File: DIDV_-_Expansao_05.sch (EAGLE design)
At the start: 83 parts, among them U101 TLC5940QPWPREP, U201 TLC5940QPWPREP

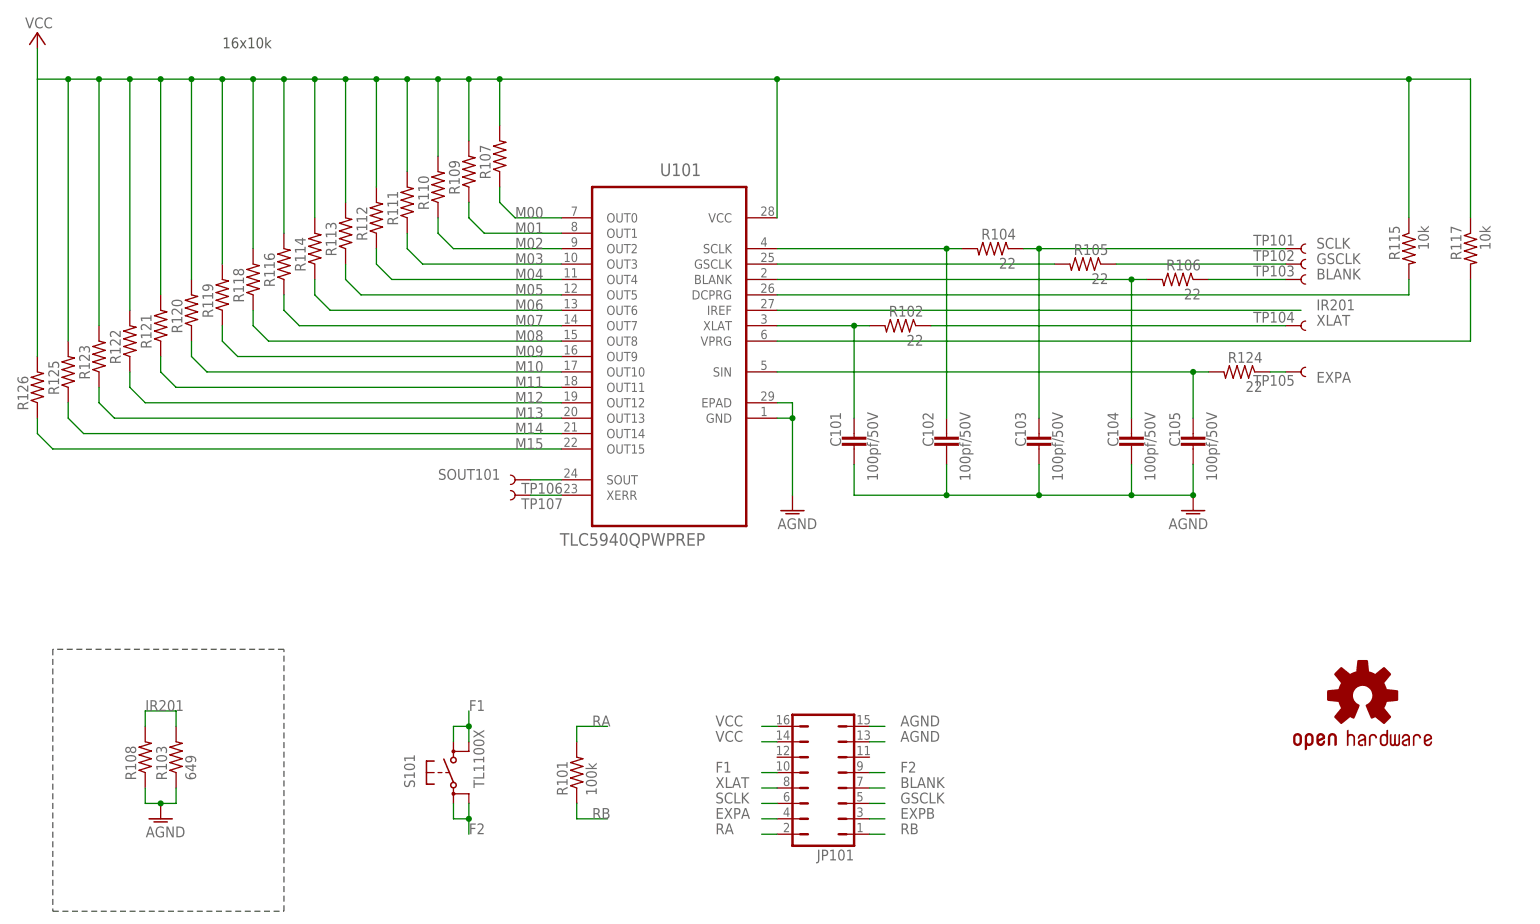
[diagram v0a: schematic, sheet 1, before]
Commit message: Revisão 7:
-  Alterações necessárias para adequação às necessidades dos exemplos de controle que temos.
-  Revisão da forma de filtragem de sinais digitais
-  Algumas nomenclaturas ainda estão erradas, deverão ser corrigidas com o andamento da implementação.
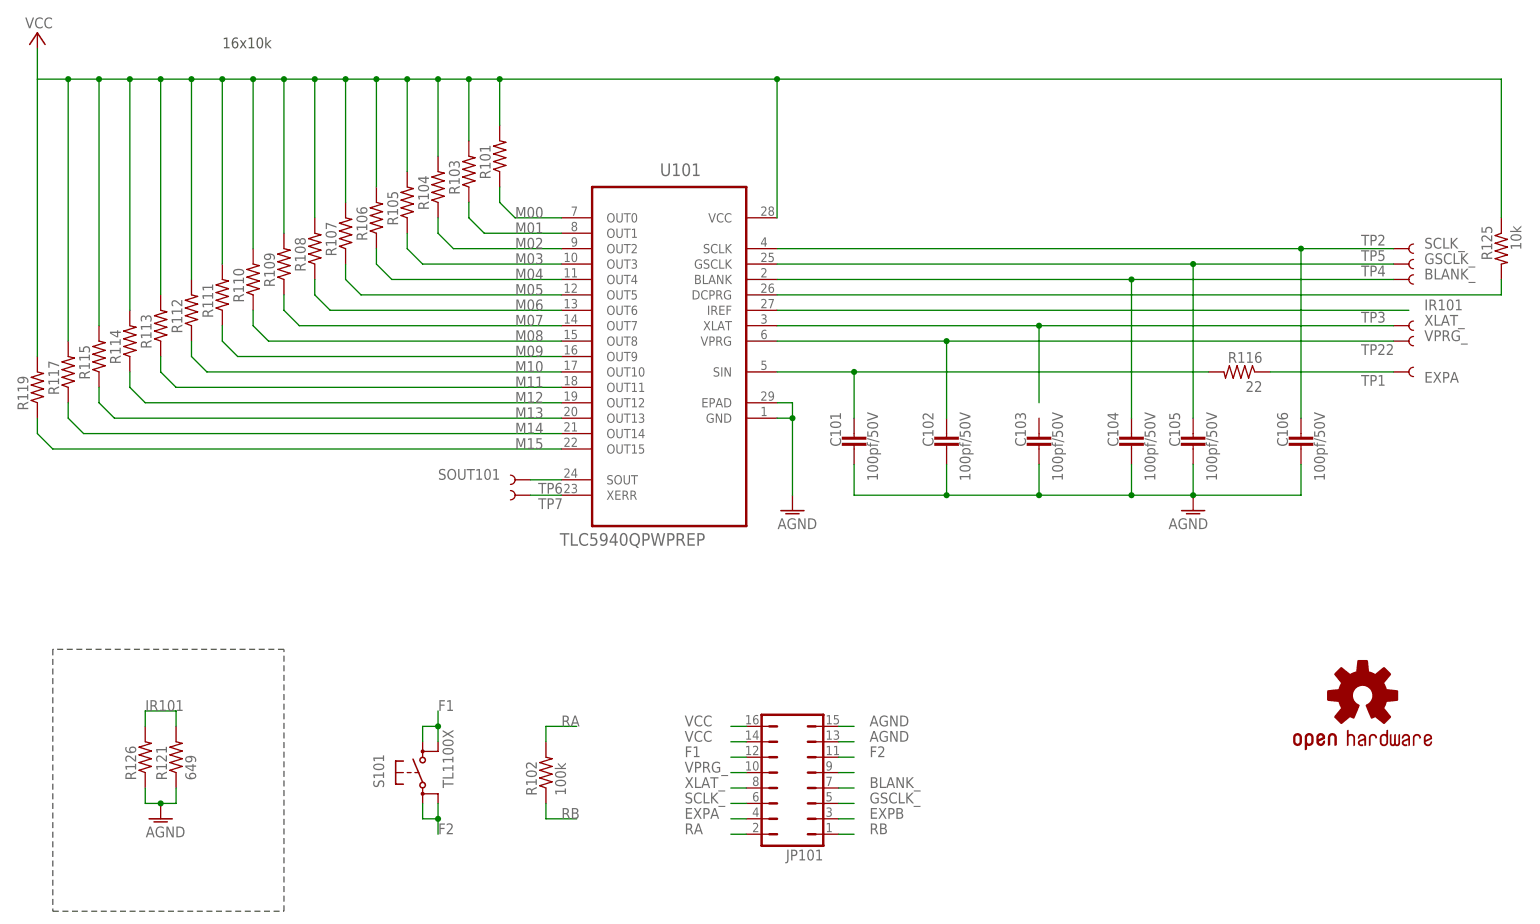
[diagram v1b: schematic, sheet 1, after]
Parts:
- removed R118, R120, R122, R123, R217: (no value), rcl:R-US_R0805
- removed R124, R222, R223: 22, rcl:R-US_R0603
- removed R219: 10k, rcl:R-US_R0603
- removed R221: 649, rcl:R-US_R0805
- removed TP101, TP102, TP103, TP104, TP105, TP15, TP16, TP17, TP18, TP19, TP20: TEST-POINT3X4, SparkFun-Passives:TEST-POINT3X4
- added C106, C207: 100pf/50V, rcl:C-EUC0603K
- added TP1, TP2, TP22, TP3, TP32, TP33, TP34, TP35, TP36, TP37, TP39, TP4, TP5: TEST-POINT3X4, SparkFun-Passives:TEST-POINT3X4
- R101: value 100k -> (none)
- R102: value 22 -> 100k; device rcl:R-US_R0603 -> rcl:R-US_R0805
- R103: value 649 -> (none)
- R104, R105, R106: value 22 -> (none); device rcl:R-US_R0603 -> rcl:R-US_R0805
- R115, R117, R218: value 10k -> (none); device rcl:R-US_R0603 -> rcl:R-US_R0805
- R116: value (none) -> 22; device rcl:R-US_R0805 -> rcl:R-US_R0603
- R121: value (none) -> 649
- R125: value (none) -> 10k; device rcl:R-US_R0805 -> rcl:R-US_R0603
- R220: value 22 -> 649; device rcl:R-US_R0603 -> rcl:R-US_R0805
- R225: value 22 -> 10k
- renumbered TP106 to TP6, TP107 to TP7, TP21 to TP38
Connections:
- removed net BLANK: JP101.7, R106.1, R224.1, TP103.1, TP18.1
- removed net GSCLK: JP101.5, R105.1, R223.1, TP102.1, TP19.1
- removed net IR501: R221.2, R226.2, U201.IREF
- removed net N$30: R105.2, U101.GSCLK
- removed net N$43: C105.2, R124.2, U101.SIN
- removed net N$47: R117.2, U101.VPRG
- removed net N$48: C104.2, R106.2, U101.BLANK
- removed net N$49: C101.2, R102.2, U101.XLAT
- removed net N$5: C102.2, R104.2, U101.SCLK
- removed net N$55: C205.2, R215.2, U201.SIN
- removed net N$57: R219.2, U201.VPRG
- removed net N$58: C202.2, R222.2, U201.SCLK
- removed net N$59: R223.2, U201.GSCLK
- removed net N$60: C204.2, R224.2, U201.BLANK
- removed net N$61: C201.2, R220.2, U201.XLAT
- removed net N$62: R218.2, U201.DCPRG
- removed net N$63: R225.1, U201.SOUT
- removed net N$64: R115.2, U101.DCPRG
- removed net SCLK: C103.2, C203.2, JP101.6, R104.1, R222.1, TP101.1, TP16.1
- removed net XLAT: JP101.8, R102.1, R220.1, TP104.1, TP17.1
- new net BLANK_: C104.2, C204.2, JP101.7, TP35.1, TP4.1, U101.BLANK, U201.BLANK
- new net GSCLK_: C105.2, C205.2, JP101.5, TP36.1, TP5.1, U101.GSCLK, U201.GSCLK
- new net IR101: R121.2, R126.2, U101.IREF
- new net N$2: JP101.9
- new net N$22: R125.2, U101.DCPRG
- new net N$39: C201.2, R215.2, U201.SIN
- new net N$4: C101.2, R116.2, U101.SIN
- new net N$69: R225.2, U201.DCPRG
- new net N$71: R224.1, U201.SOUT
- new net SCLK_: C106.2, C207.2, JP101.6, TP2.1, TP33.1, U101.SCLK, U201.SCLK
- new net VPRG_: C102.2, C202.2, JP101.10, TP22.1, TP39.1, U101.VPRG, U201.VPRG
- new net XLAT_: C203.2, JP101.8, TP3.1, TP34.1, U101.XLAT, U201.XLAT
- net AGND: now also C106.1, C207.1, R121.1, R126.1, R220.1; no longer R103.1, R108.1, R221.1
- net EXPA: now also R116.1, TP1.1; no longer R124.1, TP105.1
- net EXPB: now also R224.2, TP37.1; no longer R225.2, TP20.1
- net F1: now also JP101.12; no longer JP101.10
- net F2: now also JP101.11; no longer JP101.9
- net IR201: now also R220.2, R226.2, U201.IREF; no longer R103.2, R108.2, U101.IREF
- net M00: now also R101.1; no longer R107.1
- net M01: now also R103.1; no longer R109.1
- net M02: now also R104.1; no longer R110.1
- net M03: now also R105.1; no longer R111.1
- net M04: now also R106.1; no longer R112.1
- net M05: now also R107.1; no longer R113.1
- net M06: now also R108.1; no longer R114.1
- net M07: now also R109.1; no longer R116.1
- net M08: now also R110.1; no longer R118.1
- net M09: now also R111.1; no longer R119.1
- net M10: now also R112.1; no longer R120.1
- net M11: now also R113.1; no longer R121.1
- net M12: now also R114.1; no longer R122.1
- net M13: now also R115.1; no longer R123.1
- net M14: now also R117.1; no longer R125.1
- net M15: now also R119.1, R218.1; no longer R126.1, R217.1
- net RA: now also R102.2; no longer R101.2
- net RB: now also R102.1; no longer R101.1
- net SOUT101: now also TP32.1; no longer TP15.1
- net VCC: now also R101.2, R103.2, R104.2, R105.2, R106.2, R108.2, R115.2, R117.2, R125.1, R218.2, R225.1; no longer R115.1, R116.2, R117.1, R118.2, R120.2, R121.2, R122.2, R123.2, R125.2, R126.2, R217.2, R218.1, R219.1
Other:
- note added: "07"
- note added: "Iref - U101"
- note added: "Iref - U501"
- note removed: "06"
- note removed: "Iref - U100"
- moved on the sheet: JP101, R101, R102, R103, R104, R105, R106, R107, R108, R109, R110, R111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

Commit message: Revisão 8:
-  Add Circuito Buck
-  Alterações funcionais
-   Inserção dos primeiros boards
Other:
- note added: "08"
- note removed: "07"
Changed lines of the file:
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@@
 <text x="203.2" y="29.464" size="1.778" layer="150" font="vector">Dispositivo de Interface para</text>
 <text x="210.82" y="26.162" size="1.778" layer="150" font="vector">Deficientes Visuais</text>
-<text x="250.698" y="10.16" size="2.54" layer="150" font="vector">07</text>
+<text x="250.698" y="10.16" size="2.54" layer="150" font="vector">08</text>
 <text x="40.64" y="154.94" size="1.778" layer="97">16x10k</text>
 <text x="20.32" y="17.78" size="2.54" layer="150" font="vector">Iref - U101</text>
@@
 <text x="203.2" y="29.464" size="1.778" layer="150" font="vector">Dispositivo de Interface para</text>
 <text x="210.82" y="26.162" size="1.778" layer="150" font="vector">Deficientes Visuais</text>
-<text x="250.698" y="10.16" size="2.54" layer="150" font="vector">07</text>
+<text x="250.698" y="10.16" size="2.54" layer="150" font="vector">08</text>
 <text x="40.64" y="154.94" size="1.778" layer="97">16x10k</text>
 <text x="20.32" y="17.78" size="2.54" layer="150" font="vector">Iref - U501</text>

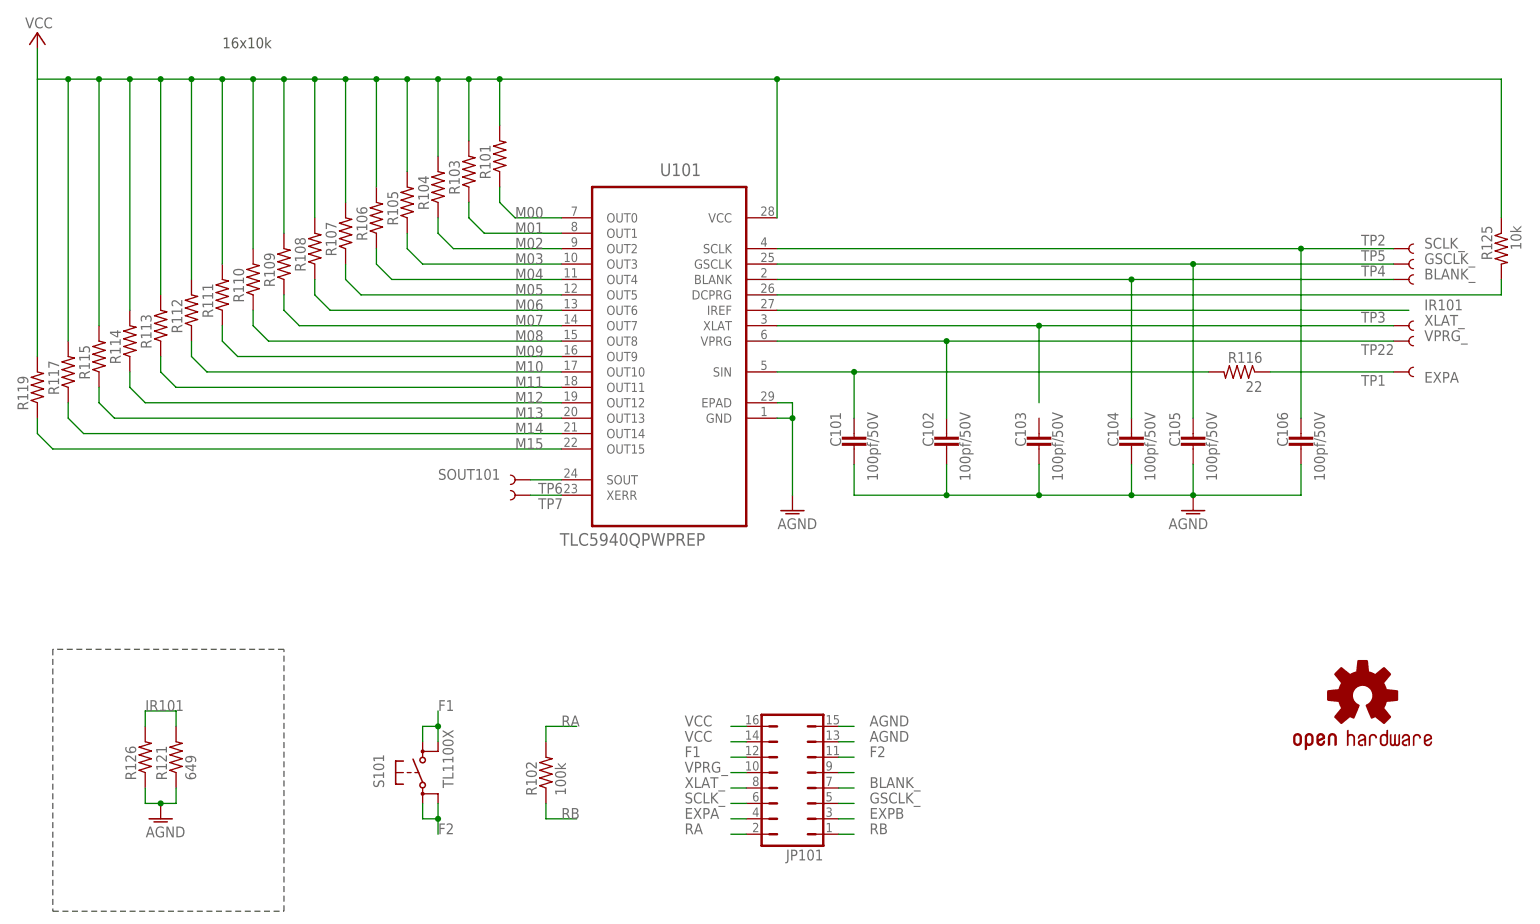
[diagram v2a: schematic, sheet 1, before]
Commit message: Revisão 9
- Corrigidos algumas falhas de ligação
- Implementação com VPRG dos TLCs via Hardware
- Inserção do cálculo do Riref

Obs. Se somente a criação de boards, não será incrementado. No caso, se criado um board novo board vou subir para 9.1 e assim por diante.
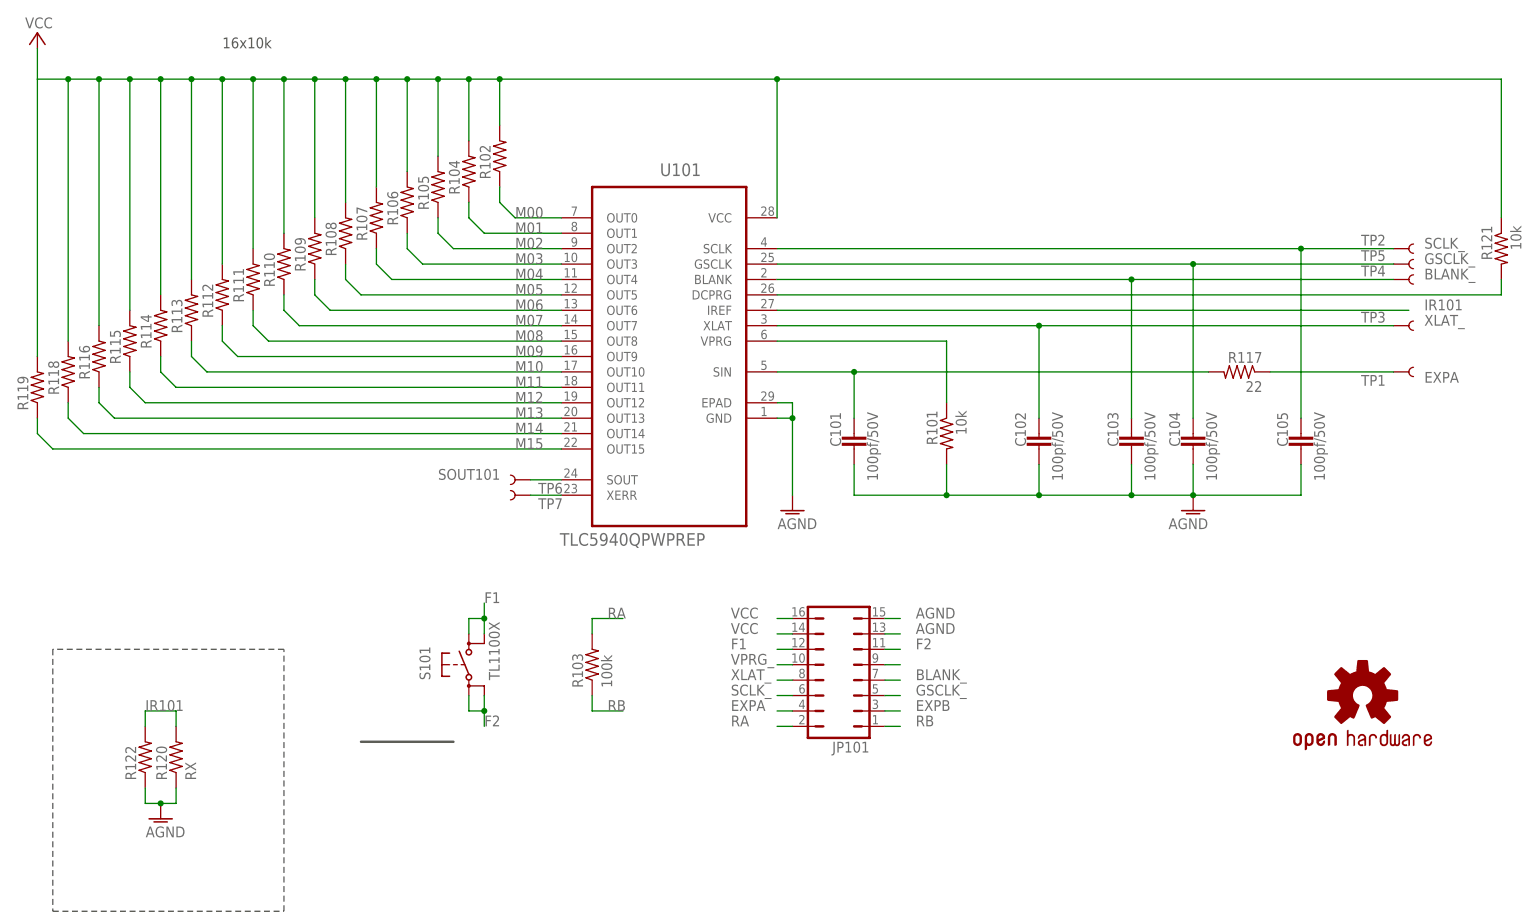
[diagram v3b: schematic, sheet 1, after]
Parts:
- removed C106, C207: 100pf/50V, rcl:C-EUC0603K
- removed R125: 10k, rcl:R-US_R0603
- removed R224: 22, rcl:R-US_R0603
- removed TP22, TP39: TEST-POINT3X4, SparkFun-Passives:TEST-POINT3X4
- added R118, R217: (no value), rcl:R-US_R0805
- added R120, R219: RX, rcl:R-US_R0805
- R101, R201: value (none) -> 10k; device rcl:R-US_R0805 -> rcl:R-US_R0603
- R102: value 100k -> (none)
- R103: value (none) -> 100k
- R116, R215: value 22 -> (none); device rcl:R-US_R0603 -> rcl:R-US_R0805
- R117, R216: value (none) -> 22; device rcl:R-US_R0805 -> rcl:R-US_R0603
- R121: value 649 -> 10k; device rcl:R-US_R0805 -> rcl:R-US_R0603
- R220: value 649 -> 22; device rcl:R-US_R0805 -> rcl:R-US_R0603
- renumbered R126 to R122, R225 to R221, R226 to R222
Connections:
- net AGND: now also R101.2, R120.1, R201.2, R219.1; no longer C106.1, C207.1, R121.1, R220.1
- net BLANK_: now also C103.2, C203.2; no longer C104.2, C204.2
- net EXPA: now also R117.1; no longer R116.1
- net EXPB: now also C205.2, R220.2; no longer C206.2, R224.2
- net GSCLK_: now also C104.2, C204.2; no longer C105.2, C205.2
- net IR101: now also R120.2; no longer R121.2
- net IR201: now also R219.2; no longer R220.2
- net M00: now also R102.1, R202.1; no longer R101.1, R201.1
- net M01: now also R104.1, R203.1; no longer R103.1, R202.1
- net M02: now also R105.1, R204.1; no longer R104.1, R203.1
- net M03: now also R106.1, R205.1; no longer R105.1, R204.1
- net M04: now also R107.1, R206.1; no longer R106.1, R205.1
- net M05: now also R108.1, R207.1; no longer R107.1, R206.1
- net M06: now also R109.1, R208.1; no longer R108.1, R207.1
- net M07: now also R110.1, R209.1; no longer R109.1, R208.1
- net M08: now also R111.1, R210.1; no longer R110.1, R209.1
- net M09: now also R112.1, R211.1; no longer R111.1, R210.1
- net M10: now also R113.1, R212.1; no longer R112.1, R211.1
- net M11: now also R114.1, R213.1; no longer R113.1, R212.1
- net M12: now also R115.1, R214.1; no longer R114.1, R213.1
- net M13: now also R116.1, R215.1; no longer R115.1, R214.1
- net M14: now also R118.1, R217.1; no longer R117.1, R216.1
- net N$22: now also R121.2; no longer R125.2
- net N$39: now also R216.2; no longer R215.2
- net N$4: now also R117.2; no longer R116.2
- net N$71: now also R220.1; no longer R224.1
- net RA: now also R103.2; no longer R102.2
- net RB: now also R103.1; no longer R102.1
- net SCLK_: now also C105.2, C206.2; no longer C106.2, C207.2
- net SOUT101: now also R216.1; no longer R215.1
- net VCC: now also R102.2, R116.2, R118.2, R121.1, R215.2, R217.2; no longer R101.2, R103.2, R117.2, R125.1, R201.2, R216.2
- net VPRG_: now also R101.1, R201.1; no longer C102.2, C202.2, TP22.1, TP39.1
- net XLAT_: now also C102.2, C202.2; no longer C203.2
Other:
- note added: "09"
- note added: "39,06"
- note added: "Imax"
- note added: "P/ RX=2k4 --> Imax=16,275mA"
- note added: "P/ RX=3k9 --> Imax=10,015mA"
- note added: "RX="
- note added: "The maximum output current per channel"
- note added: "is programmed by a single resistor."
- note removed: "08"
- moved on the sheet: C102, C103, C104, C105, C202, C203, C204, C205, C206, JP101, R101, R102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
